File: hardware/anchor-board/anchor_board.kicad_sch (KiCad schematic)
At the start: 72 parts, among them J1 USB4105-GF-A, J2 SWD 2x5 1.27mm, J3 UART TX/RX/GND, J4 GPIO breakout, J5 3V0 current shunt, J6 LED disable, J7 Reset/boot strap, J8 TC2030 SWD, SW1 SKHHALA010, U1 DWM3001C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

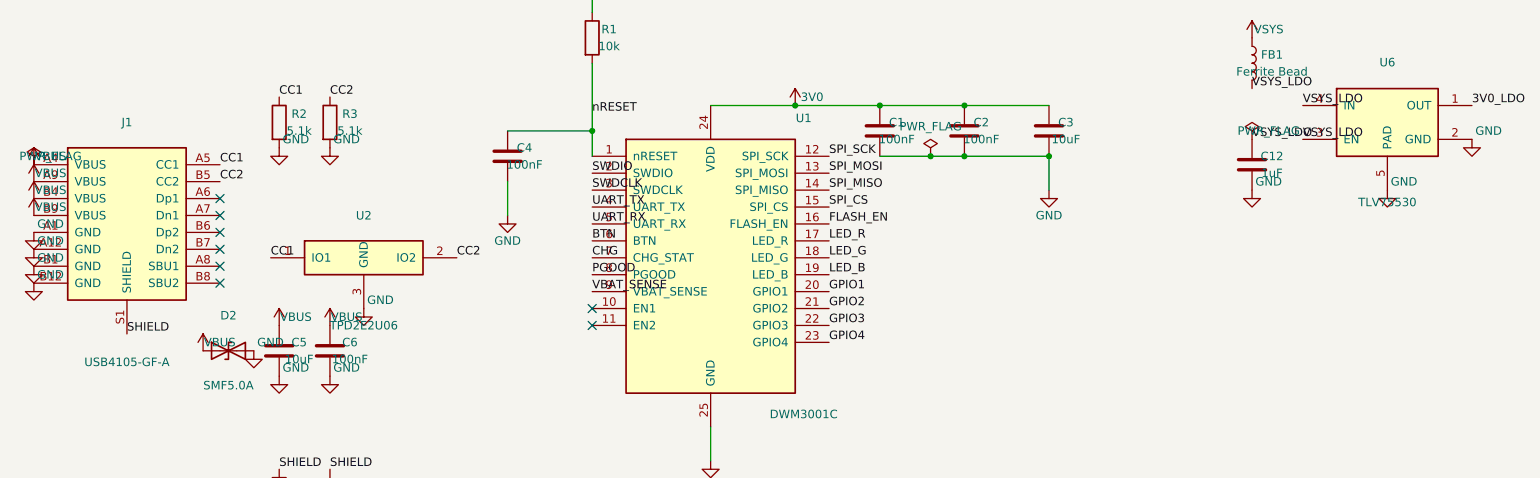
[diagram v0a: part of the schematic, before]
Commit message: Assign footprints to all anchor-board parts — schematic 0/0 ERC
Footprint assignments:
- DWM3001C: official Qorvo footprint (prior commit)
- USB-C, 18650 holder, RGB LED, TC2030 pads, BQ24074 QFN-16,
  TPS22916 WLP-4: stock KiCad library footprints
- TLV75530 X2SON-4 and Alps SKHHAL switch: new project footprints
  (land patterns approximate — flagged for verification before fab)

Symbol fixes surfaced by footprint reconciliation:
- TPD2E2U06: rebuilt as the real 6-pin SOT-563 (IO1=3, IO2=5, GND=4,
  pins 1/2/6 NC) — was a 3-pin stub
- TLV75530: dropped the spurious thermal-pad pin 5 — DQN is X2SON-4,
  no thermal pad
- USB4105: shield pin renamed S1 -> SH to match the footprint pad

ERC now passes clean: 0 errors, 0 warnings.
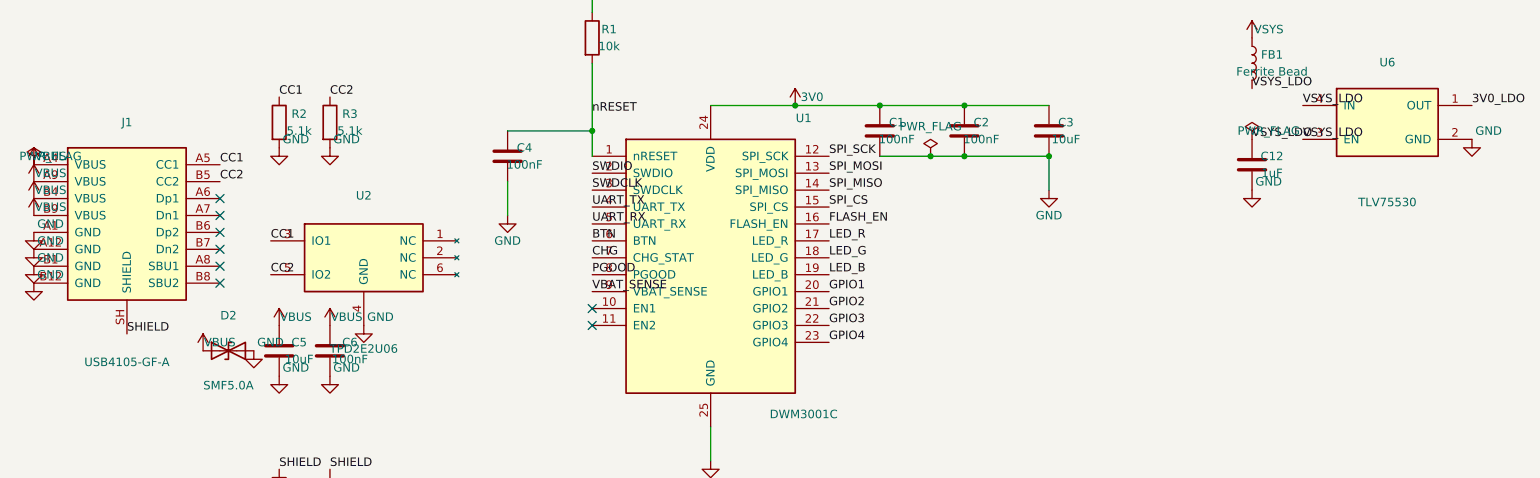
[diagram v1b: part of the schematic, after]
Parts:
- BT1: footprint infinity-stumps:Keystone_1042 -> Battery:BatteryHolder_Keystone_1042_1x18650
- D1: footprint infinity-stumps:LED_RGB_Wurth_150141 -> LED_SMD:LED_RGB_Wuerth-PLCC4_3.2x2.8mm_150141M173100
- J1: footprint infinity-stumps:USB4105-GF-A -> Connector_USB:USB_C_Receptacle_GCT_USB4105-xx-A_16P_TopMnt_Horizontal
- J8: footprint infinity-stumps:Tag-Connect_TC2030-IDC-NL -> Connector:Tag-Connect_TC2030-IDC-NL_2x03_P1.27mm_Vertical
- SW1: footprint infinity-stumps:SW_SKHHALA010 -> infinity-stumps:SW_Alps_SKHHAL
- U2: footprint infinity-stumps:TPD2E2U06_SC70 -> Package_TO_SOT_SMD:SOT-563
- U3: footprint infinity-stumps:BQ24074_QFN16 -> Package_DFN_QFN:QFN-16-1EP_3x3mm_P0.5mm_EP1.7x1.7mm
- U6: footprint infinity-stumps:TLV75530_DQN -> infinity-stumps:X2SON-4_1x1mm_P0.5mm
- U8: footprint infinity-stumps:TPS22916C_WCSP -> Package_BGA:WLP-4_0.83x0.83mm_P0.4mm
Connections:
- net CC1: now also U2.3 (IO1); no longer U2.1 (IO1)
- net CC2: now also U2.5 (IO2); no longer U2.2 (IO2)
- net GND: now also U2.4 (GND); no longer U2.3 (GND), U6.5 (PAD)
- net SHIELD: now also J1.SH (SHIELD); no longer J1.S1 (SHIELD)

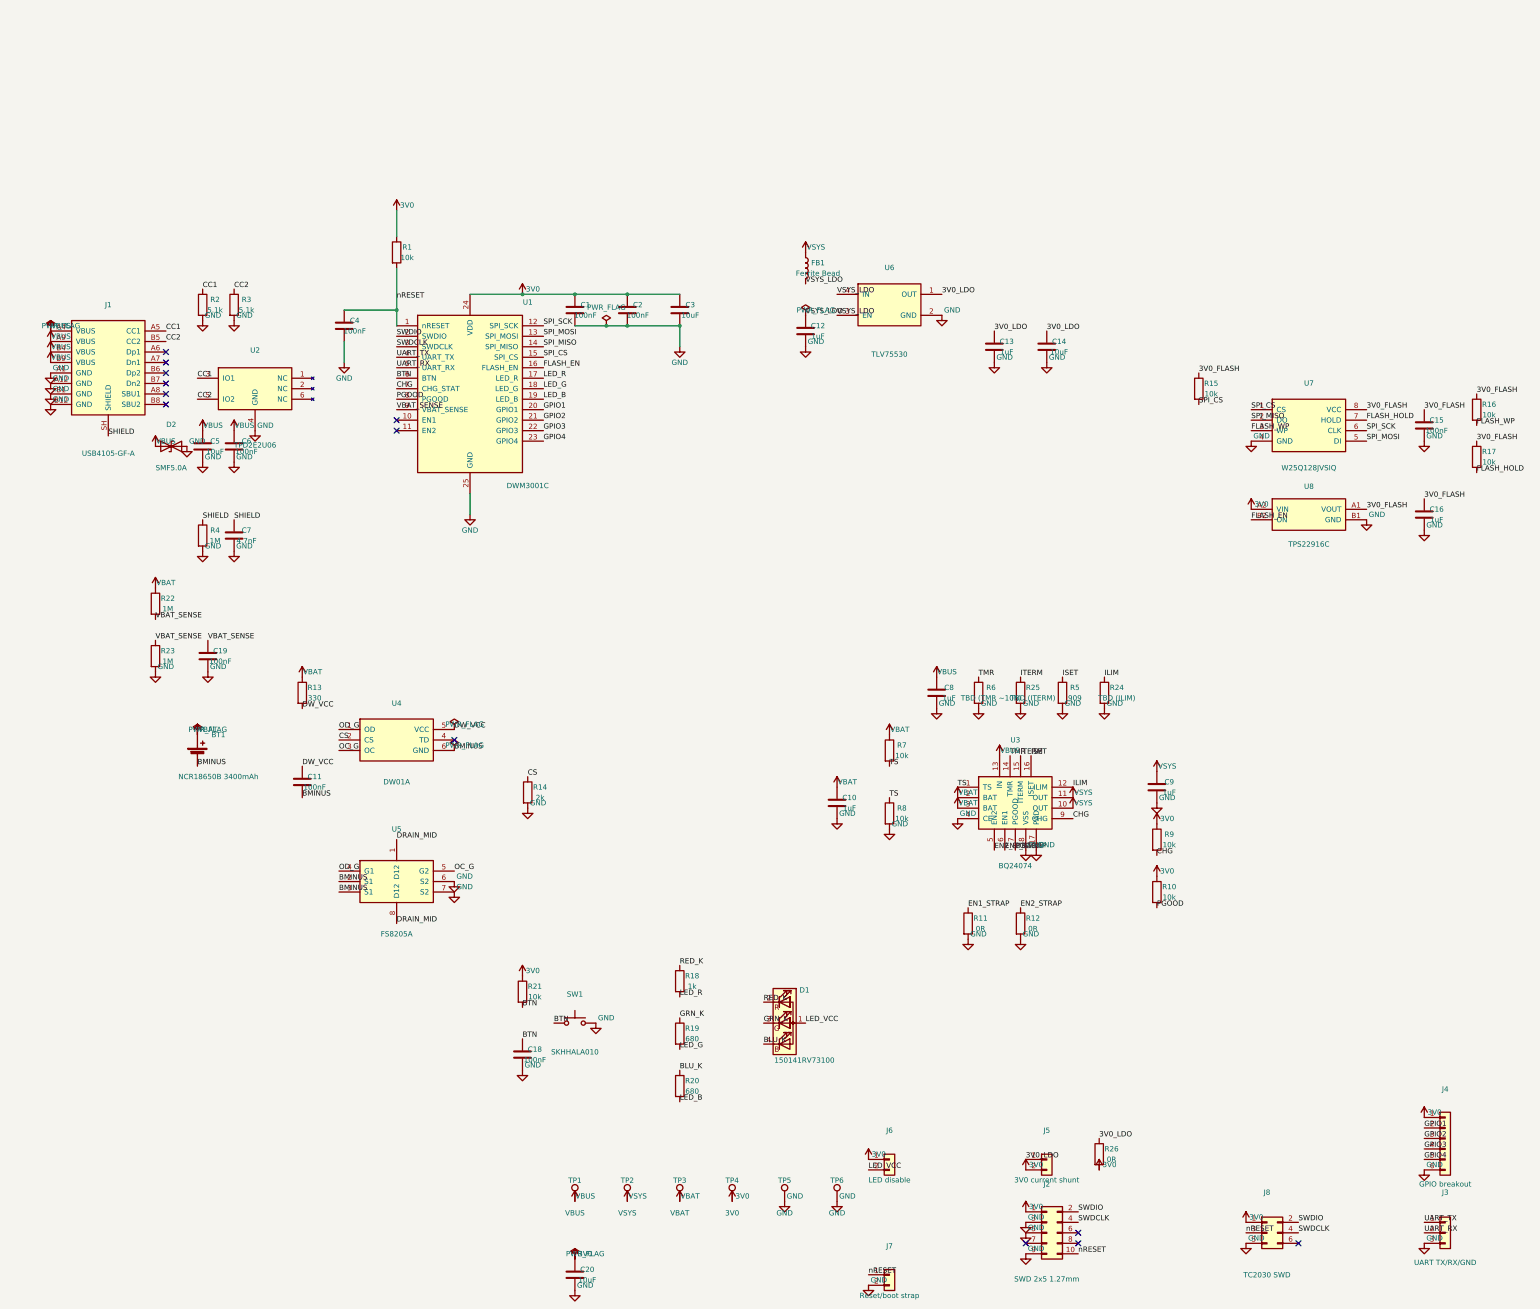
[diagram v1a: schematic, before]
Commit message: Move §4.9 + dev-rail blocks inside the A3 sheet boundary
The test points and break-off dev-rail connectors were placed at
y=287-315, off the bottom edge of the A3 sheet. Relocated both blocks
into the open area on the right side (x 305-375, y 145-245). All 72
components now sit within the sheet; ERC still 0/0.
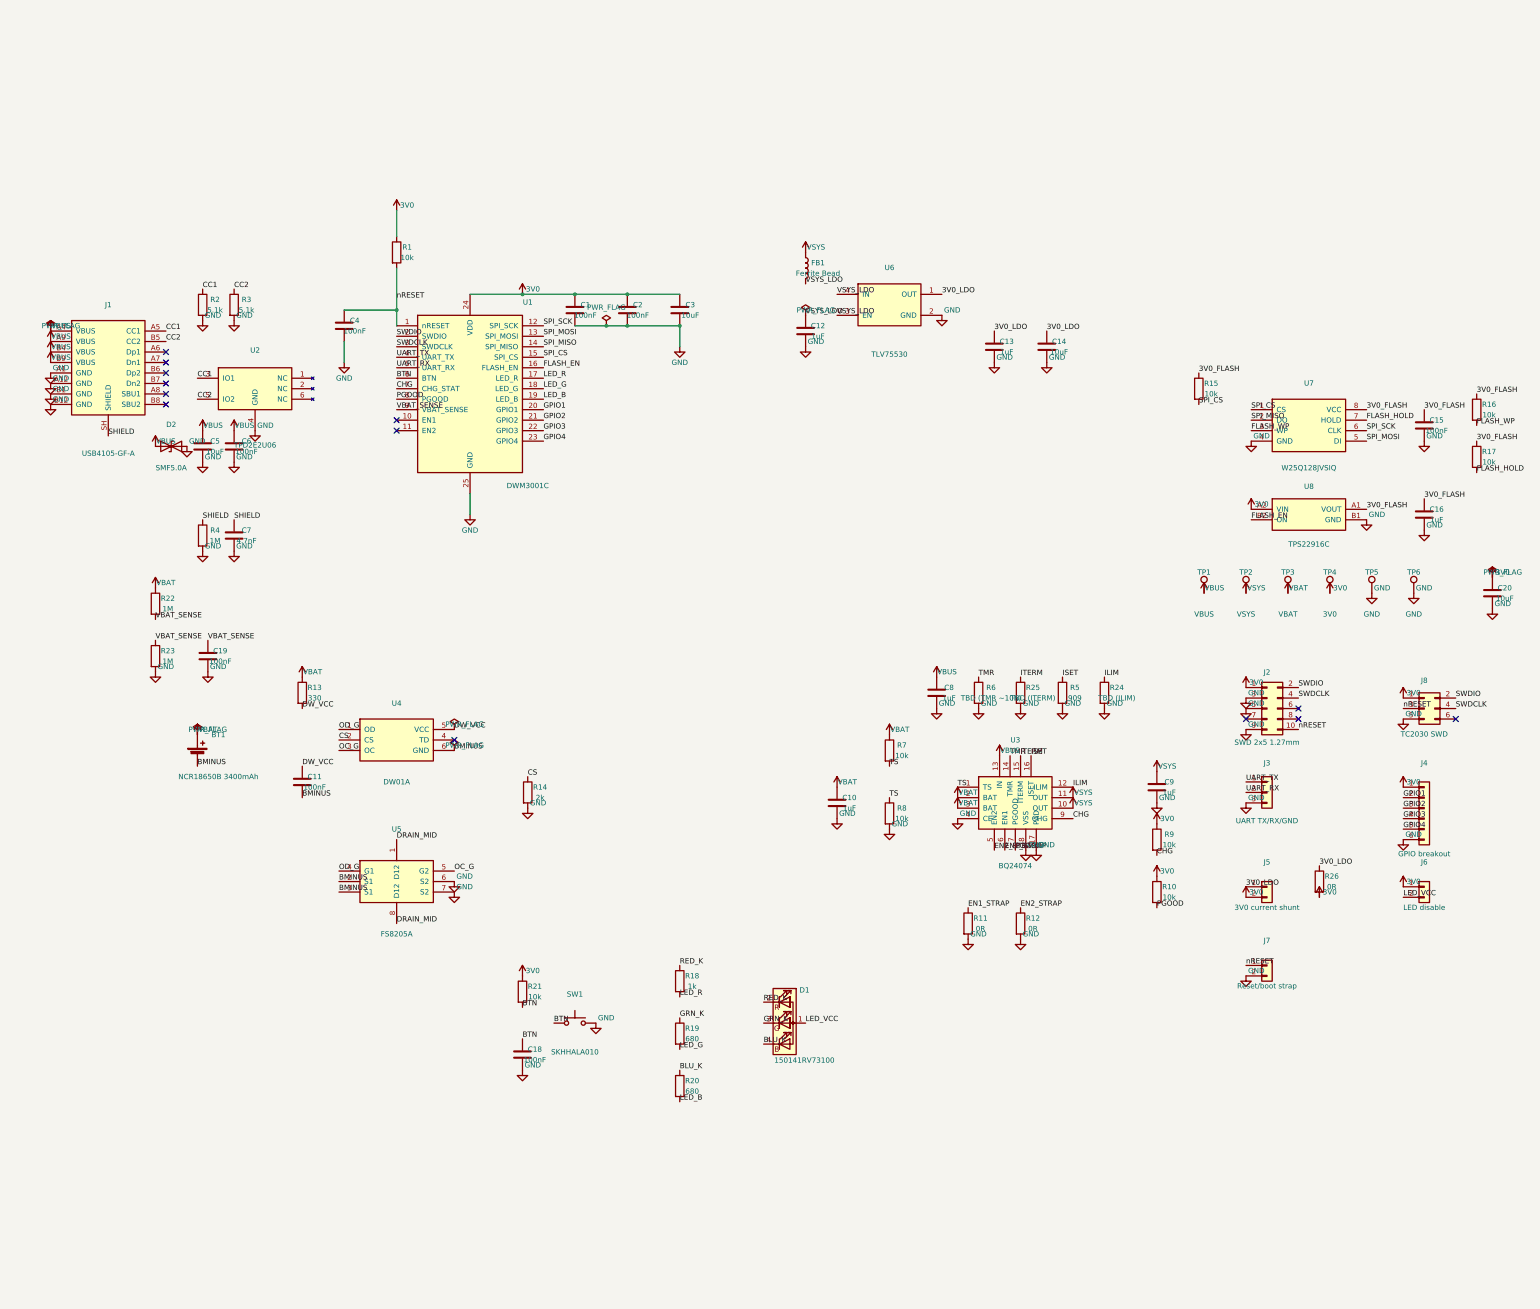
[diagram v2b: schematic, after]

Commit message: Add schematic generator to repo + stub/orient labels for readability
Moves the schematic generator out of /tmp into
hardware/anchor-board/tools/gen_schematic.py so the netlist build is
tracked. Paths are now relative to the script; the KiCad symbol dir is
overridable via $KICAD_SYMBOL_DIR.

Readability pass — every label and power port is now pulled off its pin
onto a short stub wire and oriented to read *away* from the component
body, instead of piling up on the component edge:
- labels justified by pin direction so text never runs into the body
- adjacent items in a pin column get alternating stub lengths to stagger
- collision avoidance: a stub that would touch another pin or stub is
  rejected (prevents shorting nets); a second item sharing a pin (e.g. a
  PWR_FLAG on a labelled pin) routes off perpendicular
- 204 stub wires added; ERC still 0/0

Note: re-running the generator clobbers manual layout — once the sheet
is hand-tidied in KiCad, treat the .kicad_sch as source of truth.
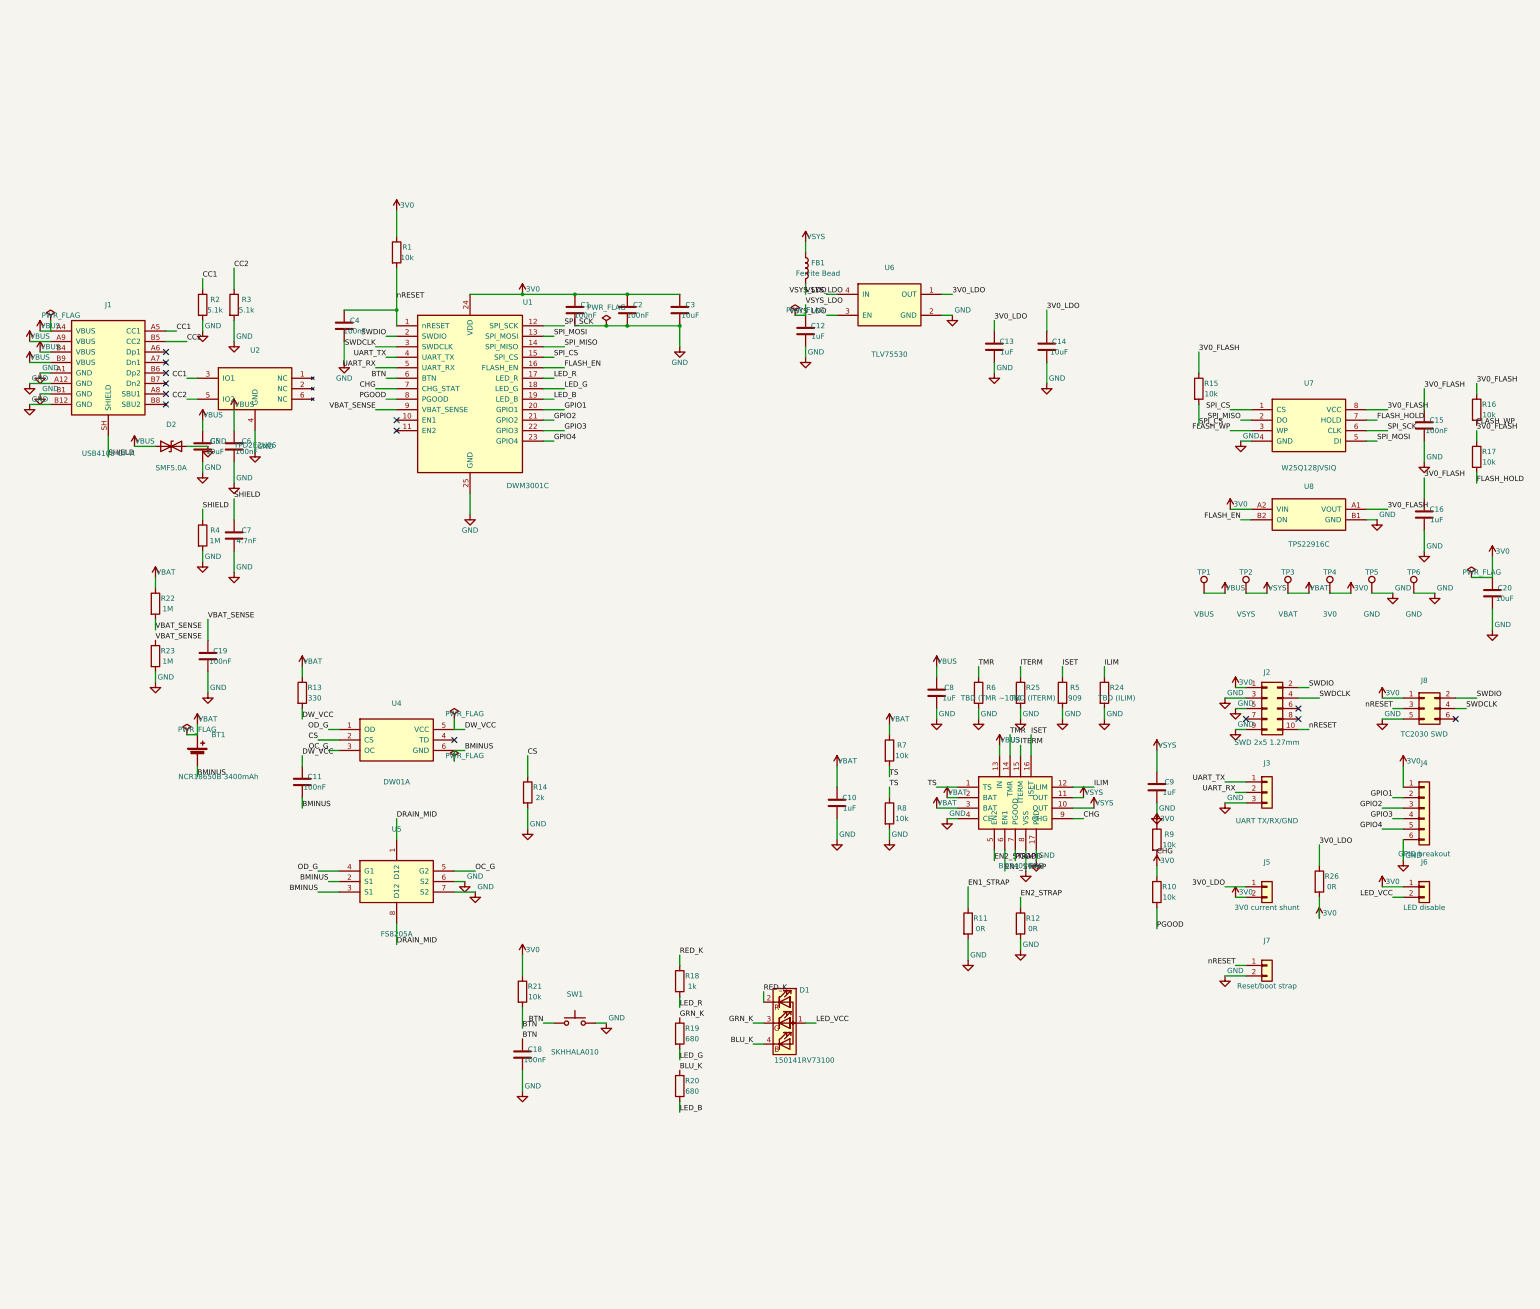
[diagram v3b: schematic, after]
